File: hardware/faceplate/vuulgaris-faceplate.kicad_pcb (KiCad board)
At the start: 4 copper layers, 298.3 x 137.8 mm, 54 parts, among them J1 HX JN2.54-2x5P TP H8.9, U1 MSP430FR2675TPT, Y1 32.768kHz FC-135 12.5pF

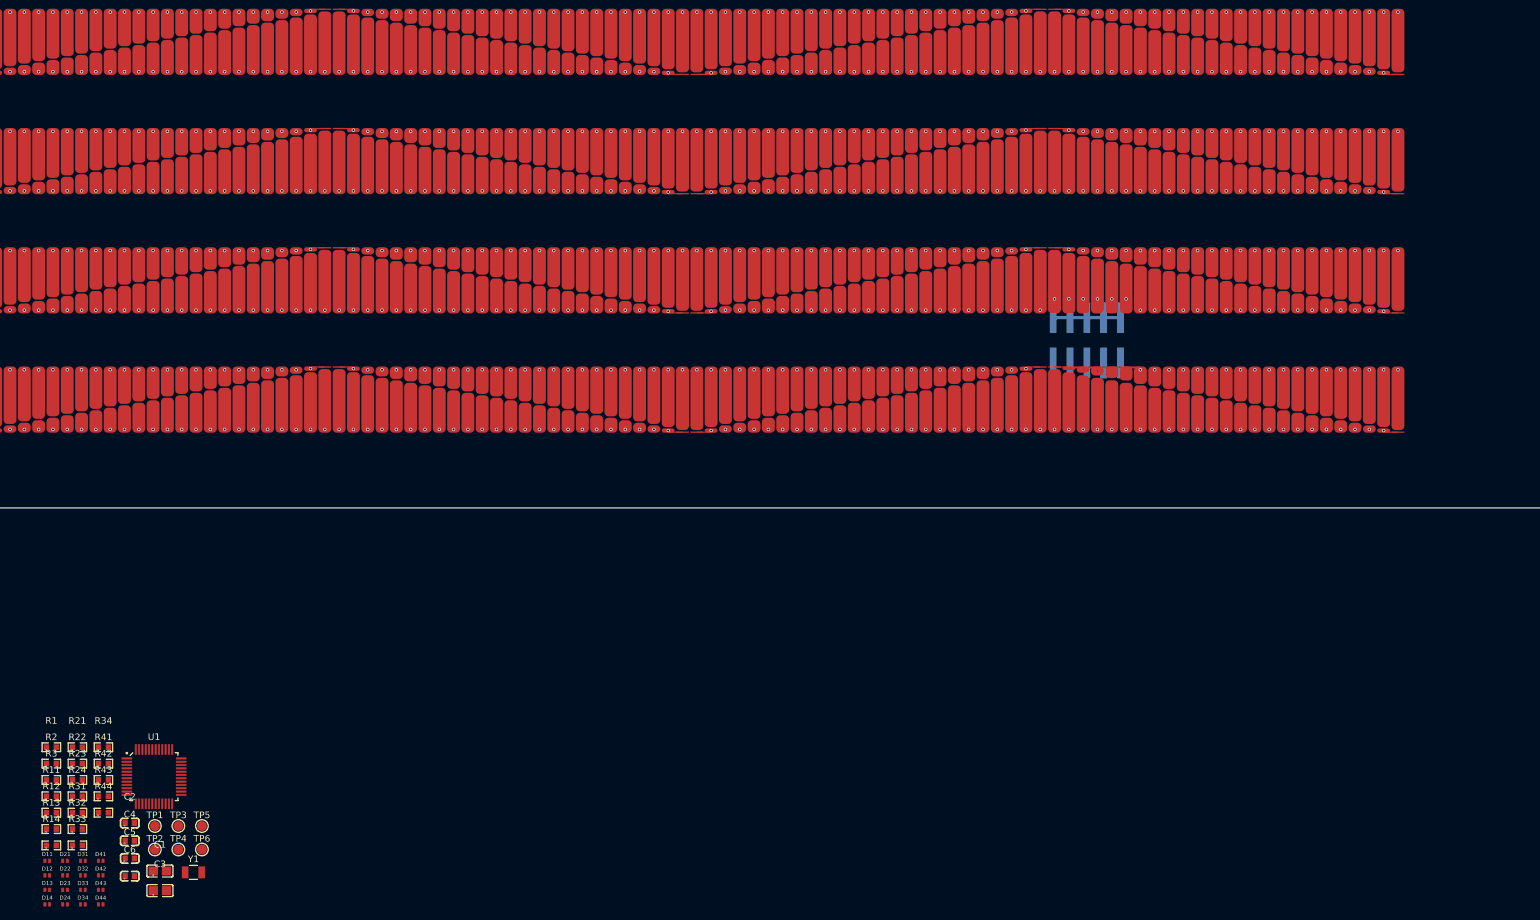
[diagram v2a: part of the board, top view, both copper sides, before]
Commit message: faceplate: place U1 and its networks in the right margin
Settled with Dylan before placing: (b) U1 in the right margin, not the
centre. ADR 0003's "centre the MCU" assumes pads around a chip; with four
stacked strips it would put pads 1 and 4's lines under pads 2 and 3 and the
MCU behind their centre printed mark. From the margin each pad's lines run
to its right end under its own pad only. (c) The UART, 3V3, RST and TEST
leave J1, which the main board fixes between pads 3 and 4, along that gap
on L4 over an L3 ground strip; firmware keeps the UART quiet during scans
(new Q23). ADR 0003's two layout rules amended to say so.

design/mkplace.py (one-shot, pcbnew) puts every part on B.Cu inside panel
x 277.6-291.3: U1 with its CAP pins facing up, the 470Rs in two
interleaved rows in pin order over them with C3 over VREG, a TVS row
beside where each pad's lines enter, C2 under pin 1, Y1 on end at the
right edge with C5/C6, C1 and the RST RC where J1's lines arrive, and
TP1-TP6 plus the UART pull-ups in the gap beside J1. U1's pin positions
were read back to confirm the orientation. Routing is Dylan's; the
README's "Layout" section says what to route and how.

Q24 records the one piece of reasoning the L2 routing leans on (buses
under same-pad elements act as if under a driven shield) until it is
confirmed against TI or on the bench.

Checked: mksch/netcheck 145/145; boardcheck parity 0, clearance 0;
DRC --unrouted 0 errors (courtyards included); panelcheck 9 OK.
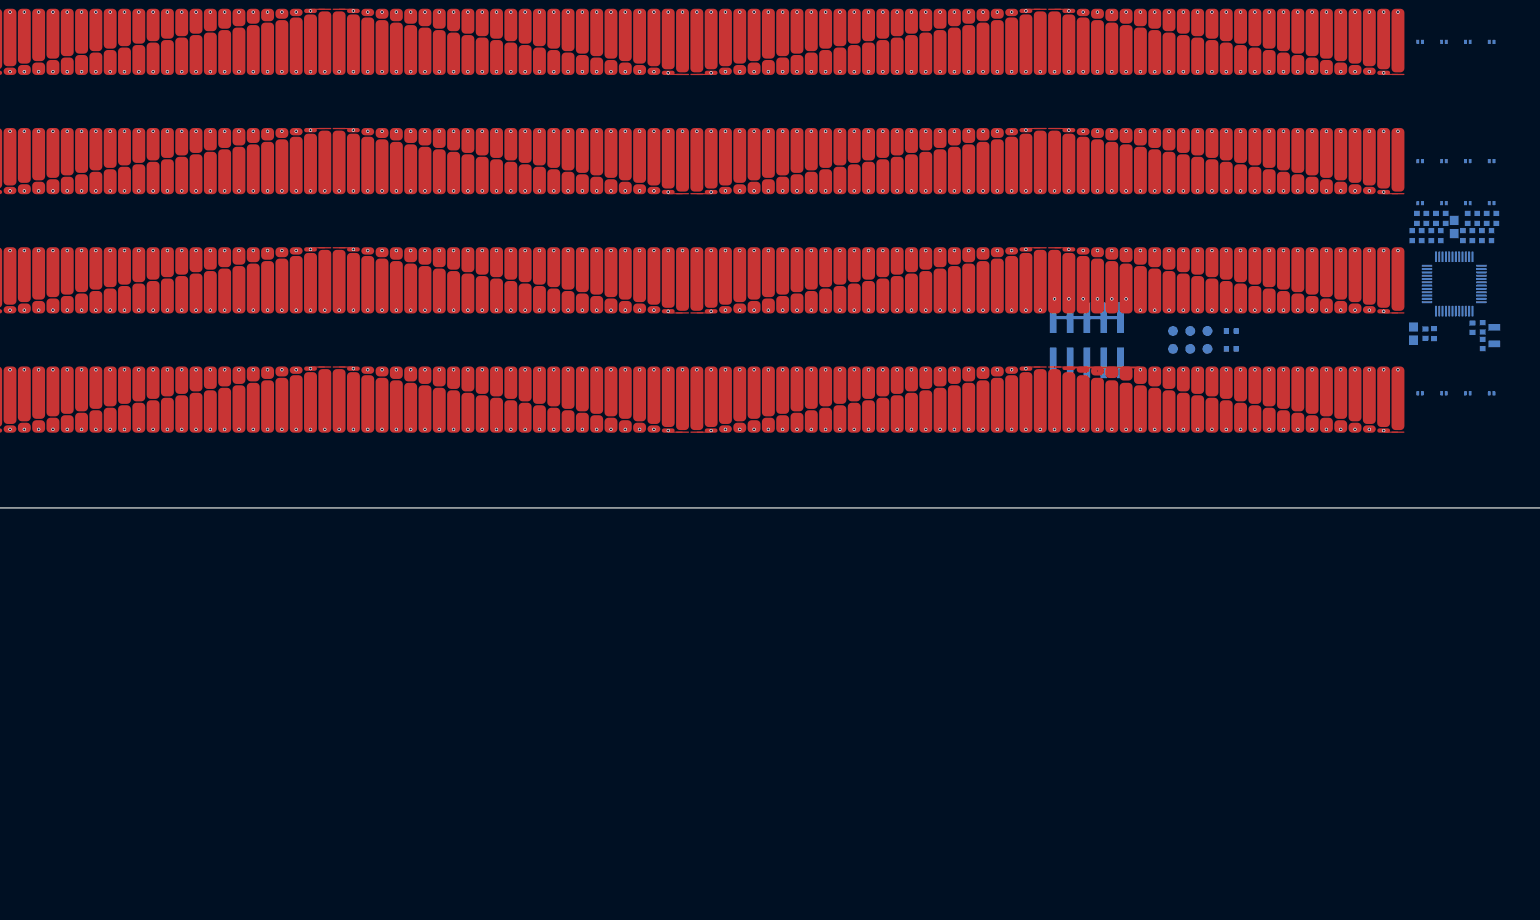
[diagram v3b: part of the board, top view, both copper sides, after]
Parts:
- C1, C2, C3, C4, C5, C6, D11, D12, D13, D14, D21, D22, D23, D24, D31, D32, D33, D34, D41, D42, D43, D44, R1, R11, R12, R13, R14, R2, R21, R22, R23, R24, R3, R31, R32, R33, R34, R41, R42, R43, R44, TP1, TP2, TP3, TP4, TP5, TP6, U1, Y1: moved to B.Cu
- moved D14 254.0 mm to (390.1, 117.5)
- moved D13 249.7 mm to (386.5, 117.5)
- moved D12 245.5 mm to (382.9, 117.5)
- moved D24 242.8 mm to (390.1, 135.5)
- moved D11 241.3 mm to (379.3, 117.5)
- moved D23 238.6 mm to (386.5, 135.5)
- moved D34 237.6 mm to (390.1, 141.8)
- moved R14 234.8 mm to (388.6, 146.7), turned to -90 degrees
- moved D22 234.4 mm to (382.9, 135.5)
- moved D33 233.4 mm to (386.5, 141.8)
- moved R13 231.1 mm to (385.8, 146.7), turned to -90 degrees
- moved D21 230.2 mm to (379.3, 135.5)
- moved R24 229.9 mm to (389.4, 144.1), turned to -90 degrees
- moved R33 229.8 mm to (387.2, 146.7), turned to -90 degrees
- moved D32 229.2 mm to (382.9, 141.8)
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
